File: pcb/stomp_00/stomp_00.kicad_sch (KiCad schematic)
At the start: 12 parts, among them J5 Conn_01x24_Pin, J6 Conn_01x24_Pin, J9 Conn_01x04_Pin, SW1 SW_DIP_x04, U7 Teensy4.1

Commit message: more input stage faffing
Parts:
- removed J9: Conn_01x04_Pin, Connector_PinHeader_2.54mm:PinHeader_1x04_P2.54mm_Vertical, symbol Connector:Conn_01x04_Pin
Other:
- removed sheet Output
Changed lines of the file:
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@@
     (stroke (width 0) (type default))
-  )
-  (text_box "OLED connector, shares I2C pins with SGTL5000"
-    (at 118.11 139.7 0) (size 25.4 10.16)
-    (stroke (width 0) (type default))
-    (fill (type none))
-    (effects (font (size 1.27 1.27)) (justify left top))
   )
   (global_label "DAC_DIN" (shape input) (at 132.08 60.96 180) (fields_autoplaced)
@@
     )
   )
-  (symbol (lib_id "Connector:Conn_01x04_Pin") (at 129.54 160.02 0) (unit 1)
-    (in_bom yes) (on_board yes) (dnp no) (fields_autoplaced)
-    (property "Reference" "J9" (at 130.175 153.67 0)
-      (effects (font (size 1.27 1.27)))
-    )
-    (property "Value" "Conn_01x04_Pin" (at 130.175 156.21 0)
-      (effects (font (size 1.27 1.27)))
-    )
-    (property "Footprint" "Connector_PinHeader_2.54mm:PinHeader_1x04_P2.54mm_Vertical" (at 129.54 160.02 0)
-      (effects (font (size 1.27 1.27)) hide)
-    )
-    (property "Datasheet" "~" (at 129.54 160.02 0)
-      (effects (font (size 1.27 1.27)) hide)
-    )
-    (pin "1")
-    (pin "2")
-    (pin "3")
-    (pin "4")
-    (instances
-      (project "stomp_00"
-        (path "/8f4a2eb0-078b-46cb-b534-a4acd11d130e"
-          (reference "J9") (unit 1)
-        )
-      )
-    )
-  )
   (symbol (lib_id "Mechanical:MountingHole") (at 214.63 30.48 0) (unit 1)
     (in_bom yes) (on_board yes) (dnp no) (fields_autoplaced)
@@
     )
   )
-  (sheet (at 20.32 115.57) (size 12.7 5.207) (fields_autoplaced)
+  (sheet (at 20.32 57.15) (size 12.7 5.207) (fields_autoplaced)
     (stroke (width 0.1524) (type solid))
     (fill (color 0 0 0 0.0000))
-    (property "Sheetname" "MIDI" (at 20.32 114.8584 0)
+    (property "Sheetname" "MIDI" (at 20.32 56.4384 0)
       (effects (font (size 1.27 1.27)) (justify left bottom))
     )
-    (property "Sheetfile" "midi.kicad_sch" (at 20.32 121.3616 0)
+    (property "Sheetfile" "midi.kicad_sch" (at 20.32 62.9416 0)
       (effects (font (size 1.27 1.27)) (justify left top))
     )
@@
     )
   )
-  (sheet (at 20.32 22.733) (size 12.7 5.207) (fields_autoplaced)
+  (sheet (at 20.32 24.638) (size 12.7 5.207) (fields_autoplaced)
     (stroke (width 0.1524) (type solid))
     (fill (color 0 0 0 0.0000))
-    (property "Sheetname" "Power" (at 20.32 22.0214 0)
+    (property "Sheetname" "Power" (at 20.32 23.9264 0)
       (effects (font (size 1.27 1.27)) (justify left bottom))
     )
-    (property "Sheetfile" "power.kicad_sch" (at 20.32 28.5246 0)
+    (property "Sheetfile" "power.kicad_sch" (at 20.32 30.4296 0)
       (effects (font (size 1.27 1.27)) (justify left top))
     )
@@
     )
   )
-  (sheet (at 20.32 60.96) (size 12.7 5.207) (fields_autoplaced)
+  (sheet (at 20.32 46.355) (size 12.7 5.207) (fields_autoplaced)
     (stroke (width 0.1524) (type solid))
     (fill (color 0 0 0 0.0000))
-    (property "Sheetname" "DAC" (at 20.32 60.2484 0)
+    (property "Sheetname" "DAC" (at 20.32 45.6434 0)
       (effects (font (size 1.27 1.27)) (justify left bottom))
     )
-    (property "Sheetfile" "dac.kicad_sch" (at 20.32 66.7516 0)
+    (property "Sheetfile" "dac.kicad_sch" (at 20.32 52.1466 0)
       (effects (font (size 1.27 1.27)) (justify left top))
     )
@@
       )
     )
-  )
-  (sheet (at 20.32 48.26) (size 12.7 5.207) (fields_autoplaced)
-    (stroke (width 0.1524) (type solid))
-    (fill (color 0 0 0 0.0000))
-    (property "Sheetname" "Output" (at 20.32 47.5484 0)
-      (effects (font (size 1.27 1.27)) (justify left bottom))
-    )
-    (property "Sheetfile" "output.kicad_sch" (at 20.32 54.0516 0)
-      (effects (font (size 1.27 1.27)) (justify left top))
-    )
-    (instances
-      (project "stomp_00"
-        (path "/8f4a2eb0-078b-46cb-b534-a4acd11d130e" (page "4"))
-      )
-    )

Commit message: good progress with physical layout
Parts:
- removed J5, J6: Conn_01x24_Pin, Connector_PinHeader_2.54mm:PinHeader_1x24_P2.54mm_Vertical, symbol Connector:Conn_01x24_Pin
- added J8: Conn_01x09_Pin, Connector_PinHeader_2.54mm:PinHeader_1x09_P2.54mm_Vertical, symbol Connector:Conn_01x09_Pin
- added JP1: Jumper_2_Bridged, symbol Jumper:Jumper_2_Bridged
- added SW2: Footswitch, stomp:Footswitch_3PDT, symbol stomp:SW_3PDT
- U7: footprint teensy:Teensy41 -> stomp:Teensy41_stomp
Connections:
- new net: J8.1 (Pin_1), SW2.1 (A)
- new net: J8.2 (Pin_2), SW2.2 (B)
- new net: J8.3 (Pin_3), SW2.3 (C)
- new net: J8.4 (Pin_4), SW2.4 (A)
- new net: J8.5 (Pin_5), SW2.5 (B)
- new net: J8.6 (Pin_6), SW2.6 (C)
- new net: J8.7 (Pin_7), SW2.7 (A)
- new net: J8.8 (Pin_8), SW2.8 (B)
- new net: J8.9 (Pin_9), SW2.9 (C)
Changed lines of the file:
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@@
     (stroke (width 0) (type default))
+  )
+  (wire (pts (xy 43.18 138.43) (xy 43.18 107.95))
+    (stroke (width 0) (type default))
+  )
+  (wire (pts (xy 57.15 115.57) (xy 80.01 115.57))
+    (stroke (width 0) (type default))
+  )
+  (wire (pts (xy 60.96 130.81) (xy 80.01 130.81))
+    (stroke (width 0) (type default))
+  )
+  (wire (pts (xy 46.99 118.11) (xy 45.72 118.11))
+    (stroke (width 0) (type default))
+  )
+  (wire (pts (xy 57.15 120.65) (xy 80.01 120.65))
+    (stroke (width 0) (type default))
+  )
+  (wire (pts (xy 43.18 107.95) (xy 76.2 107.95))
+    (stroke (width 0) (type default))
+  )
+  (wire (pts (xy 76.2 133.35) (xy 80.01 133.35))
+    (stroke (width 0) (type default))
+  )
+  (wire (pts (xy 45.72 110.49) (xy 78.74 110.49))
+    (stroke (width 0) (type default))
+  )
+  (wire (pts (xy 44.45 128.27) (xy 44.45 109.22))
+    (stroke (width 0) (type default))
+  )
+  (wire (pts (xy 58.42 123.19) (xy 80.01 123.19))
+    (stroke (width 0) (type default))
+  )
+  (wire (pts (xy 46.99 138.43) (xy 43.18 138.43))
+    (stroke (width 0) (type default))
+  )
+  (wire (pts (xy 57.15 135.89) (xy 60.96 135.89))
+    (stroke (width 0) (type default))
+  )
+  (wire (pts (xy 78.74 118.11) (xy 80.01 118.11))
+    (stroke (width 0) (type default))
+  )
+  (wire (pts (xy 77.47 125.73) (xy 80.01 125.73))
+    (stroke (width 0) (type default))
+  )
+  (wire (pts (xy 60.96 135.89) (xy 60.96 130.81))
+    (stroke (width 0) (type default))
+  )
+  (wire (pts (xy 62.23 135.89) (xy 80.01 135.89))
+    (stroke (width 0) (type default))
+  )
+  (wire (pts (xy 77.47 109.22) (xy 77.47 125.73))
+    (stroke (width 0) (type default))
+  )
+  (wire (pts (xy 45.72 118.11) (xy 45.72 110.49))
+    (stroke (width 0) (type default))
+  )
+  (wire (pts (xy 57.15 140.97) (xy 62.23 140.97))
+    (stroke (width 0) (type default))
+  )
+  (wire (pts (xy 58.42 125.73) (xy 58.42 123.19))
+    (stroke (width 0) (type default))
+  )
+  (wire (pts (xy 57.15 130.81) (xy 59.69 130.81))
+    (stroke (width 0) (type default))
+  )
+  (wire (pts (xy 46.99 128.27) (xy 44.45 128.27))
+    (stroke (width 0) (type default))
+  )
+  (wire (pts (xy 62.23 140.97) (xy 62.23 135.89))
+    (stroke (width 0) (type default))
+  )
+  (wire (pts (xy 59.69 130.81) (xy 59.69 128.27))
+    (stroke (width 0) (type default))
+  )
+  (wire (pts (xy 78.74 110.49) (xy 78.74 118.11))
+    (stroke (width 0) (type default))
+  )
+  (wire (pts (xy 59.69 128.27) (xy 80.01 128.27))
+    (stroke (width 0) (type default))
+  )
+  (wire (pts (xy 44.45 109.22) (xy 77.47 109.22))
+    (stroke (width 0) (type default))
+  )
+  (wire (pts (xy 57.15 125.73) (xy 58.42 125.73))
+    (stroke (width 0) (type default))
+  )
+  (wire (pts (xy 76.2 107.95) (xy 76.2 133.35))
+    (stroke (width 0) (type default))
+  )
+  (text_box "Add default routing with cuttable traces:\n\n1: 7\n2: guitar input tip\n3: circuit audio input\n\n4: not connected\n5: ground\n6: led negative\n\n7: 1\n8: guitar output tip\n9: circuit audio output"
+    (at 46.99 146.05 0) (size 43.18 30.48)
+    (stroke (width 0) (type default))
+    (fill (type none))
+    (effects (font (size 1.27 1.27)) (justify left top))
   )
   (global_label "DAC_DIN" (shape input) (at 132.08 60.96 180) (fields_autoplaced)
@@
     )
   )
+  (symbol (lib_id "Connector:Conn_01x09_Pin") (at 85.09 125.73 0) (mirror y) (unit 1)
+    (in_bom yes) (on_board yes) (dnp no) (fields_autoplaced)
+    (property "Reference" "J8" (at 85.8012 125.0863 0)
+      (effects (font (size 1.27 1.27)) (justify right))
+    )
+    (property "Value" "Conn_01x09_Pin" (at 85.8012 127.0073 0)
+      (effects (font (size 1.27 1.27)) (justify right))
+    )
+    (property "Footprint" "Connector_PinHeader_2.54mm:PinHeader_1x09_P2.54mm_Vertical" (at 85.09 125.73 0)
+      (effects (font (size 1.27 1.27)) hide)
+    )
+    (property "Datasheet" "~" (at 85.09 125.73 0)
+      (effects (font (size 1.27 1.27)) hide)
+    )
+    (pin "1")
+    (pin "2")
+    (pin "3")
+    (pin "4")
+    (pin "5")
+    (pin "6")
+    (pin "7")
+    (pin "8")
+    (pin "9")
+    (instances
+      (project "stomp_00"
+        (path "/8f4a2eb0-078b-46cb-b534-a4acd11d130e"
+          (reference "J8") (unit 1)
+        )
+      )
+    )
+  )
   (symbol (lib_id "teensy:Teensy4.1") (at 160.02 95.25 0) (unit 1)
     (in_bom yes) (on_board yes) (dnp no) (fields_autoplaced)
@@
       (effects (font (size 1.27 1.27)))
     )
-    (property "Footprint" "teensy:Teensy41" (at 149.86 85.09 0)
+    (property "Footprint" "stomp:Teensy41_stomp" (at 149.86 85.09 0)
       (effects (font (size 1.27 1.27)) hide)
     )
@@
     )
   )
-  (symbol (lib_id "Connector:Conn_01x24_Pin") (at 203.2 68.58 0) (mirror y) (unit 1)
-    (in_bom yes) (on_board yes) (dnp no)
-    (property "Reference" "J6" (at 202.565 36.83 0)
-      (effects (font (size 1.27 1.27)))
-    )
-    (property "Value" "Conn_01x24_Pin" (at 202.565 39.37 0)
-      (effects (font (size 1.27 1.27)))
-    )
-    (property "Footprint" "Connector_PinHeader_2.54mm:PinHeader_1x24_P2.54mm_Vertical" (at 203.2 68.58 0)
-      (effects (font (size 1.27 1.27)) hide)
-    )
-    (property "Datasheet" "~" (at 203.2 68.58 0)
-      (effects (font (size 1.27 1.27)) hide)
-    )
-    (pin "1")
-    (pin "10")
-    (pin "11")
-    (pin "12")
-    (pin "13")
-    (pin "14")
-    (pin "15")
-    (pin "16")
-    (pin "17")
-    (pin "18")
-    (pin "19")
-    (pin "2")
-    (pin "20")
-    (pin "21")
-    (pin "22")
-    (pin "23")
-    (pin "24")
+  (symbol (lib_name "SW_3PDT_1") (lib_id "stomp:SW_3PDT") (at 52.07 128.27 0) (unit 2)
+    (in_bom yes) (on_board yes) (dnp no) (fields_autoplaced)
+    (property "Reference" "SW2" (at 52.07 122.3391 0)
+      (effects (font (size 1.27 1.27)))
+    )
+    (property "Value" "Footswitch" (at 52.07 124.2601 0)
+      (effects (font (size 1.27 1.27)))
+    )
+    (property "Footprint" "stomp:Footswitch_3PDT" (at 52.07 128.27 0)
+      (effects (font (size 1.27 1.27)) hide)
+    )
+    (property "Datasheet" "~" (at 52.07 128.27 0)
+      (effects (font (size 1.27 1.27)) hide)
+    )
+    (pin "1")
+    (pin "2")
     (pin "3")
     (pin "4")
@@
       (project "stomp_00"
         (path "/8f4a2eb0-078b-46cb-b534-a4acd11d130e"
-          (reference "J6") (unit 1)
+          (reference "SW2") (unit 2)
         )
       )
@@
     )
   )
-  (symbol (lib_id "Connector:Conn_01x24_Pin") (at 111.76 68.58 0) (unit 1)
-    (in_bom yes) (on_board yes) (dnp no) (fields_autoplaced)
-    (property "Reference" "J5" (at 112.395 36.83 0)
-      (effects (font (size 1.27 1.27)))
-    )
-    (property "Value" "Conn_01x24_Pin" (at 112.395 39.37 0)
-      (effects (font (size 1.27 1.27)))
-    )
-    (property "Footprint" "Connector_PinHeader_2.54mm:PinHeader_1x24_P2.54mm_Vertical" (at 111.76 68.58 0)
-      (effects (font (size 1.27 1.27)) hide)
-    )
-    (property "Datasheet" "~" (at 111.76 68.58 0)
-      (effects (font (size 1.27 1.27)) hide)
-    )
-    (pin "1")
-    (pin "10")
-    (pin "11")
-    (pin "12")
-    (pin "13")
-    (pin "14")
-    (pin "15")
-    (pin "16")
-    (pin "17")
-    (pin "18")
-    (pin "19")
-    (pin "2")
-    (pin "20")
-    (pin "21")
-    (pin "22")
-    (pin "23")
-    (pin "24")
+  (symbol (lib_id "stomp:SW_3PDT") (at 52.07 118.11 0) (unit 1)
+    (in_bom yes) (on_board yes) (dnp no) (fields_autoplaced)
+    (property "Reference" "SW2" (at 52.07 112.1791 0)
+      (effects (font (size 1.27 1.27)))
+    )
+    (property "Value" "Footswitch" (at 52.07 114.1001 0)
+      (effects (font (size 1.27 1.27)))
+    )
+    (property "Footprint" "stomp:Footswitch_3PDT" (at 52.07 118.11 0)
+      (effects (font (size 1.27 1.27)) hide)
+    )
+    (property "Datasheet" "~" (at 52.07 118.11 0)
+      (effects (font (size 1.27 1.27)) hide)
+    )
+    (pin "1")
+    (pin "2")
     (pin "3")
     (pin "4")
@@
       (project "stomp_00"
         (path "/8f4a2eb0-078b-46cb-b534-a4acd11d130e"
-          (reference "J5") (unit 1)
+          (reference "SW2") (unit 1)
         )
       )
@@
         )
       )
+    )
+  )
+  (symbol (lib_id "Jumper:Jumper_2_Bridged") (at 76.2 90.17 0) (unit 1)
+    (in_bom yes) (on_board yes) (dnp no) (fields_autoplaced)
+    (property "Reference" "JP1" (at 76.2 86.5251 0)
+      (effects (font (size 1.27 1.27)))
+    )
+    (property "Value" "Jumper_2_Bridged" (at 76.2 88.4461 0)
+      (effects (font (size 1.27 1.27)))
+    )
+    (property "Footprint" "" (at 76.2 90.17 0)
+      (effects (font (size 1.27 1.27)) hide)
+    )
+    (property "Datasheet" "~" (at 76.2 90.17 0)
+      (effects (font (size 1.27 1.27)) hide)
+    )
+    (pin "1")
+    (pin "2")
+    (instances
+      (project "stomp_00"
+        (path "/8f4a2eb0-078b-46cb-b534-a4acd11d130e"
+          (reference "JP1") (unit 1)
+        )
+      )
+    )
+  )
+  (symbol (lib_name "SW_3PDT_2") (lib_id "stomp:SW_3PDT") (at 52.07 138.43 0) (unit 3)
+    (in_bom yes) (on_board yes) (dnp no) (fields_autoplaced)
+    (property "Reference" "SW2" (at 52.07 132.4991 0)
+      (effects (font (size 1.27 1.27)))
+    )
+    (property "Value" "Footswitch" (at 52.07 134.4201 0)
+      (effects (font (size 1.27 1.27)))
+    )
+    (property "Footprint" "stomp:Footswitch_3PDT" (at 52.07 138.43 0)
+      (effects (font (size 1.27 1.27)) hide)
+    )
+    (property "Datasheet" "~" (at 52.07 138.43 0)
+      (effects (font (size 1.27 1.27)) hide)
+    )
+    (pin "1")
+    (pin "2")
+    (pin "3")
+    (pin "4")
+    (pin "5")
+    (pin "6")
+    (pin "7")
+    (pin "8")
+    (pin "9")
+    (instances
+      (project "stomp_00"
+        (path "/8f4a2eb0-078b-46cb-b534-a4acd11d130e"
+          (reference "SW2") (unit 3)
+        )
+      )

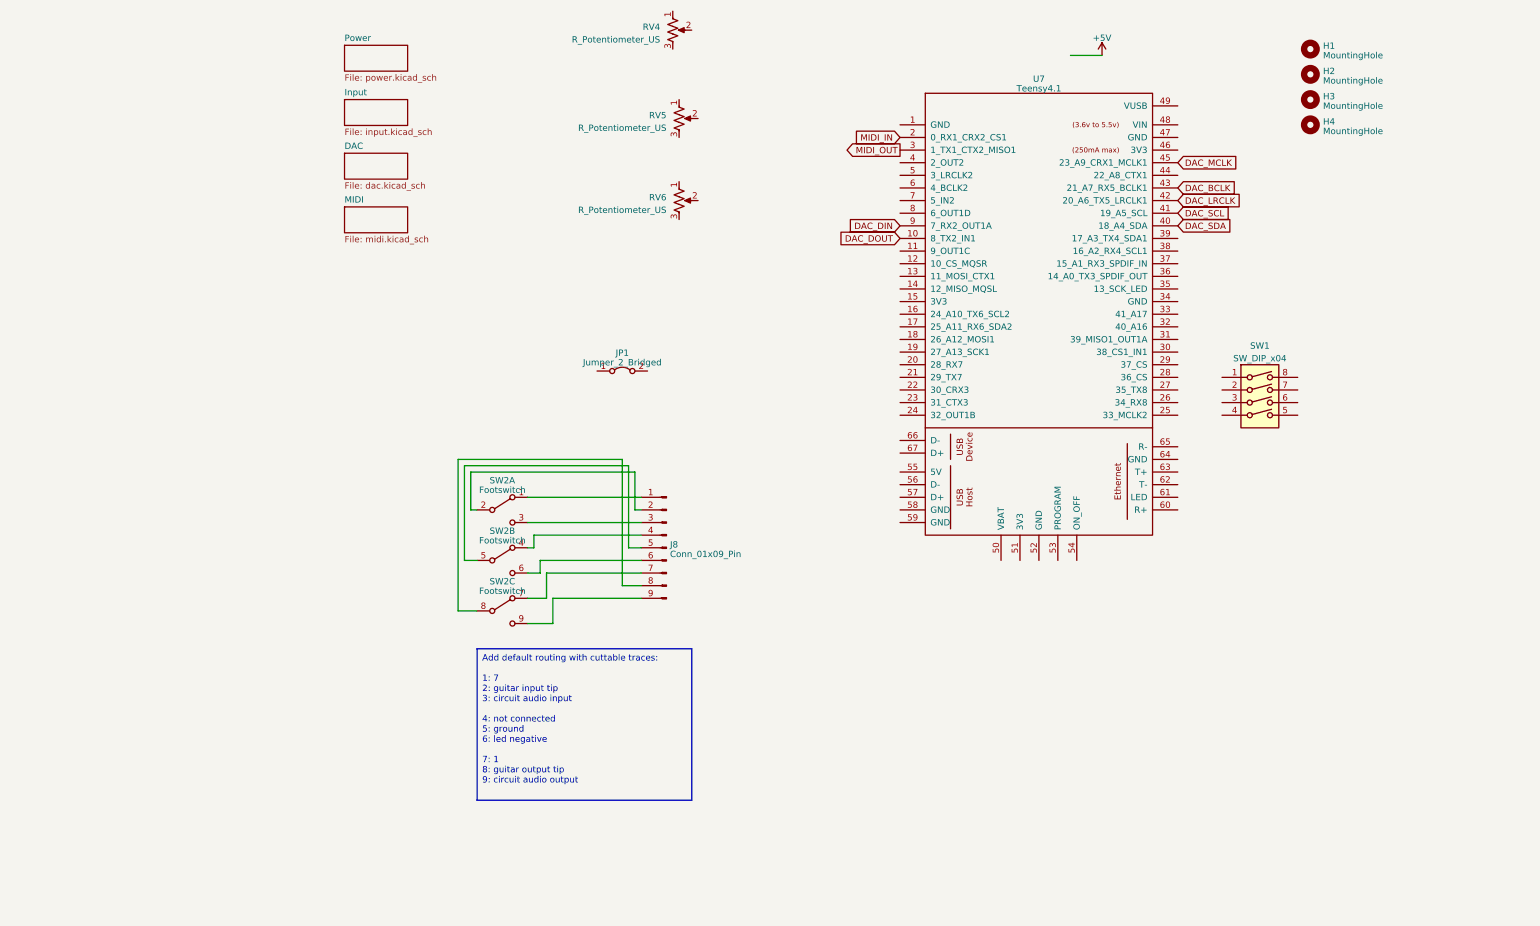
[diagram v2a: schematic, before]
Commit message: footswitch routing
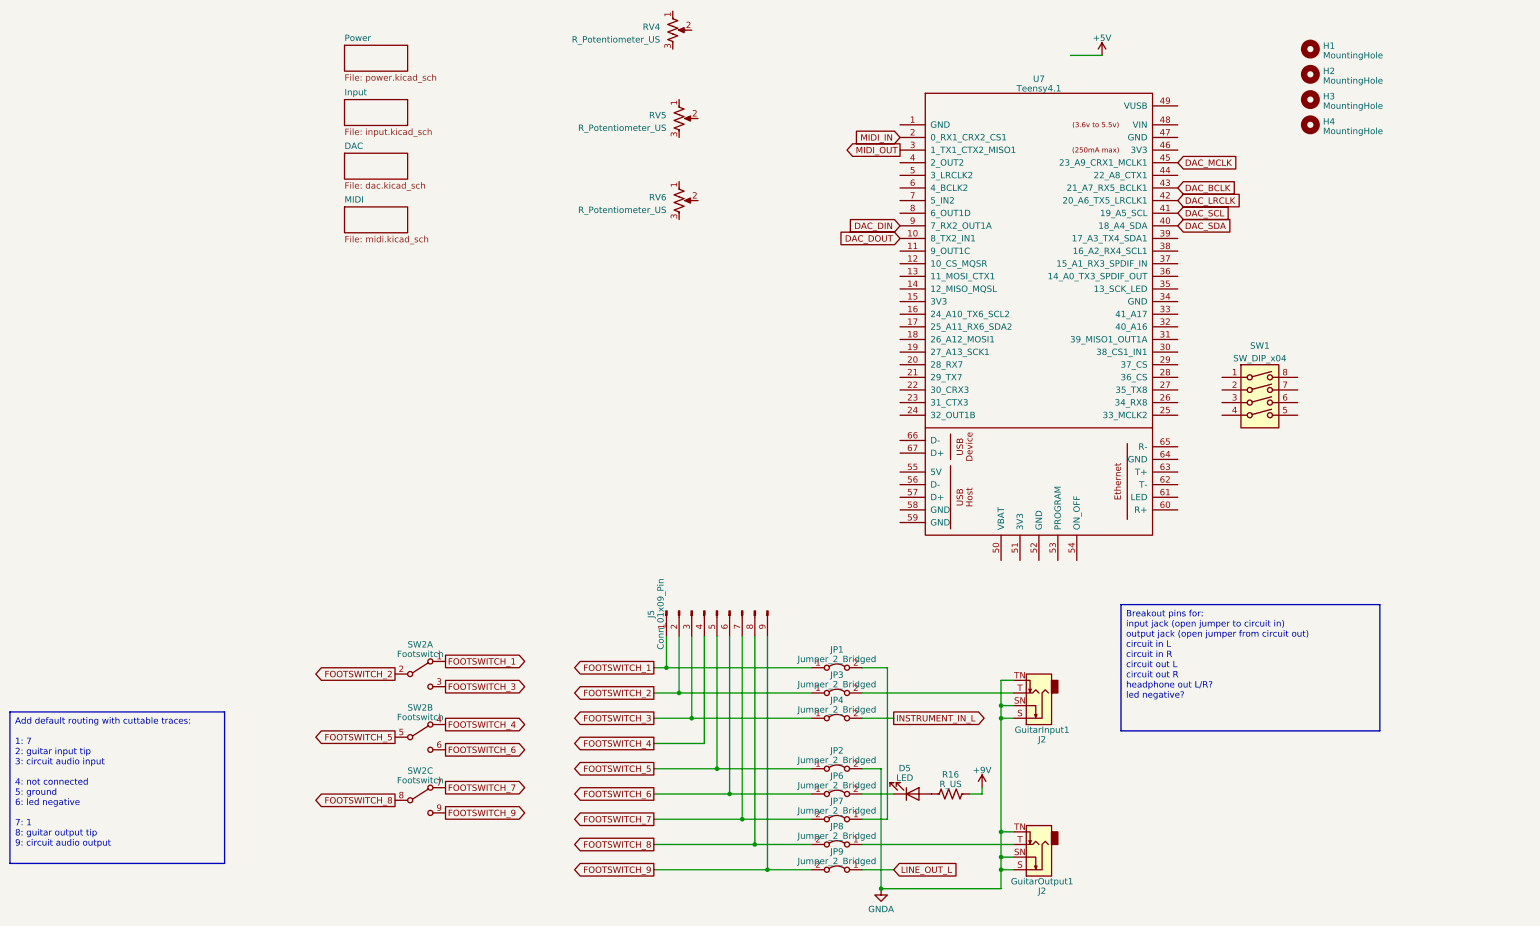
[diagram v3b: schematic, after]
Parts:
- removed J8: Conn_01x09_Pin, Connector_PinHeader_2.54mm:PinHeader_1x09_P2.54mm_Vertical, symbol Connector:Conn_01x09_Pin
- added D5: LED, LED_THT:LED_D5.0mm, symbol Device:LED
- added J2: GuitarInput1, Connector_Audio:Jack_6.35mm_Neutrik_NMJ4HCD2_Horizontal, symbol Connector_Audio:NMJ4HCD2
- added J2: GuitarOutput1, Connector_Audio:Jack_6.35mm_Neutrik_NMJ4HCD2_Horizontal, symbol Connector_Audio:NMJ4HCD2
- added J5: Conn_01x09_Pin, Connector_PinHeader_2.54mm:PinHeader_1x09_P2.54mm_Vertical, symbol Connector:Conn_01x09_Pin
- added JP2, JP3, JP4, JP6, JP7, JP8, JP9: Jumper_2_Bridged, Jumper:SolderJumper-2_P1.3mm_Bridged2Bar_RoundedPad1.0x1.5mm, symbol Jumper:Jumper_2_Bridged
- added R16: R_US, Resistor_THT:R_Axial_DIN0207_L6.3mm_D2.5mm_P7.62mm_Horizontal, symbol Device:R_US
- JP1: footprint (none) -> Jumper:SolderJumper-2_P1.3mm_Bridged2Bar_RoundedPad1.0x1.5mm
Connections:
- net FOOTSWITCH_1: now reaches SW2.1 (A)
- net FOOTSWITCH_1: now also JP1.1 (A), J5.1 (Pin_1)
- net FOOTSWITCH_2: now reaches SW2.2 (B)
- net FOOTSWITCH_2: now also J5.2 (Pin_2), JP3.1 (A)
- net FOOTSWITCH_3: now reaches SW2.3 (C)
- net FOOTSWITCH_3: now also J5.3 (Pin_3), JP4.1 (A)
- net FOOTSWITCH_4: now reaches SW2.4 (A)
- net FOOTSWITCH_4: now also J5.4 (Pin_4)
- net FOOTSWITCH_5: now reaches SW2.5 (B)
- net FOOTSWITCH_5: now also J5.5 (Pin_5), JP2.1 (A)
- net FOOTSWITCH_6: now reaches SW2.6 (C)
- net FOOTSWITCH_6: now also J5.6 (Pin_6), JP6.1 (A)
- net FOOTSWITCH_7: now reaches SW2.7 (A)
- net FOOTSWITCH_7: now also J5.7 (Pin_7), JP7.2 (B)
- net FOOTSWITCH_8: now reaches SW2.8 (B)
- net FOOTSWITCH_8: now also J5.8 (Pin_8), JP8.2 (B)
- net FOOTSWITCH_9: now reaches SW2.9 (C)
- net FOOTSWITCH_9: now also J5.9 (Pin_9), JP9.2 (B)
- net at JP1.2 (B): now also JP7.1 (A)
- new net: J2.T, JP8.1 (A)
- new net: J2.T, JP3.2 (B)
- new net: D5.1 (K), JP6.2 (B)
- new net: D5.2 (A), R16.1
- new net +9V: R16.2
- new net GNDA: J2.S, J2.S, J2.SN, J2.SN, J2.TN, J2.TN, JP2.2 (B)
- new net INSTRUMENT_IN_L: JP4.2 (B)
- new net LINE_OUT_L: JP9.1 (A)
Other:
- moved on the sheet: JP1, SW2A, SW2B, SW2C
